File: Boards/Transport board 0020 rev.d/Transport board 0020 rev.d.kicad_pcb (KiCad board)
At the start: 2 copper layers, 165.9 x 187.4 mm, 82 parts, among them P1 CEC card edge connector large, U1 TR1602, U10 LM311, U11 LM741, U12 LM311, U14 Spare, U15 Spare, U2 6821, U3 DM8602N, U4 7410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

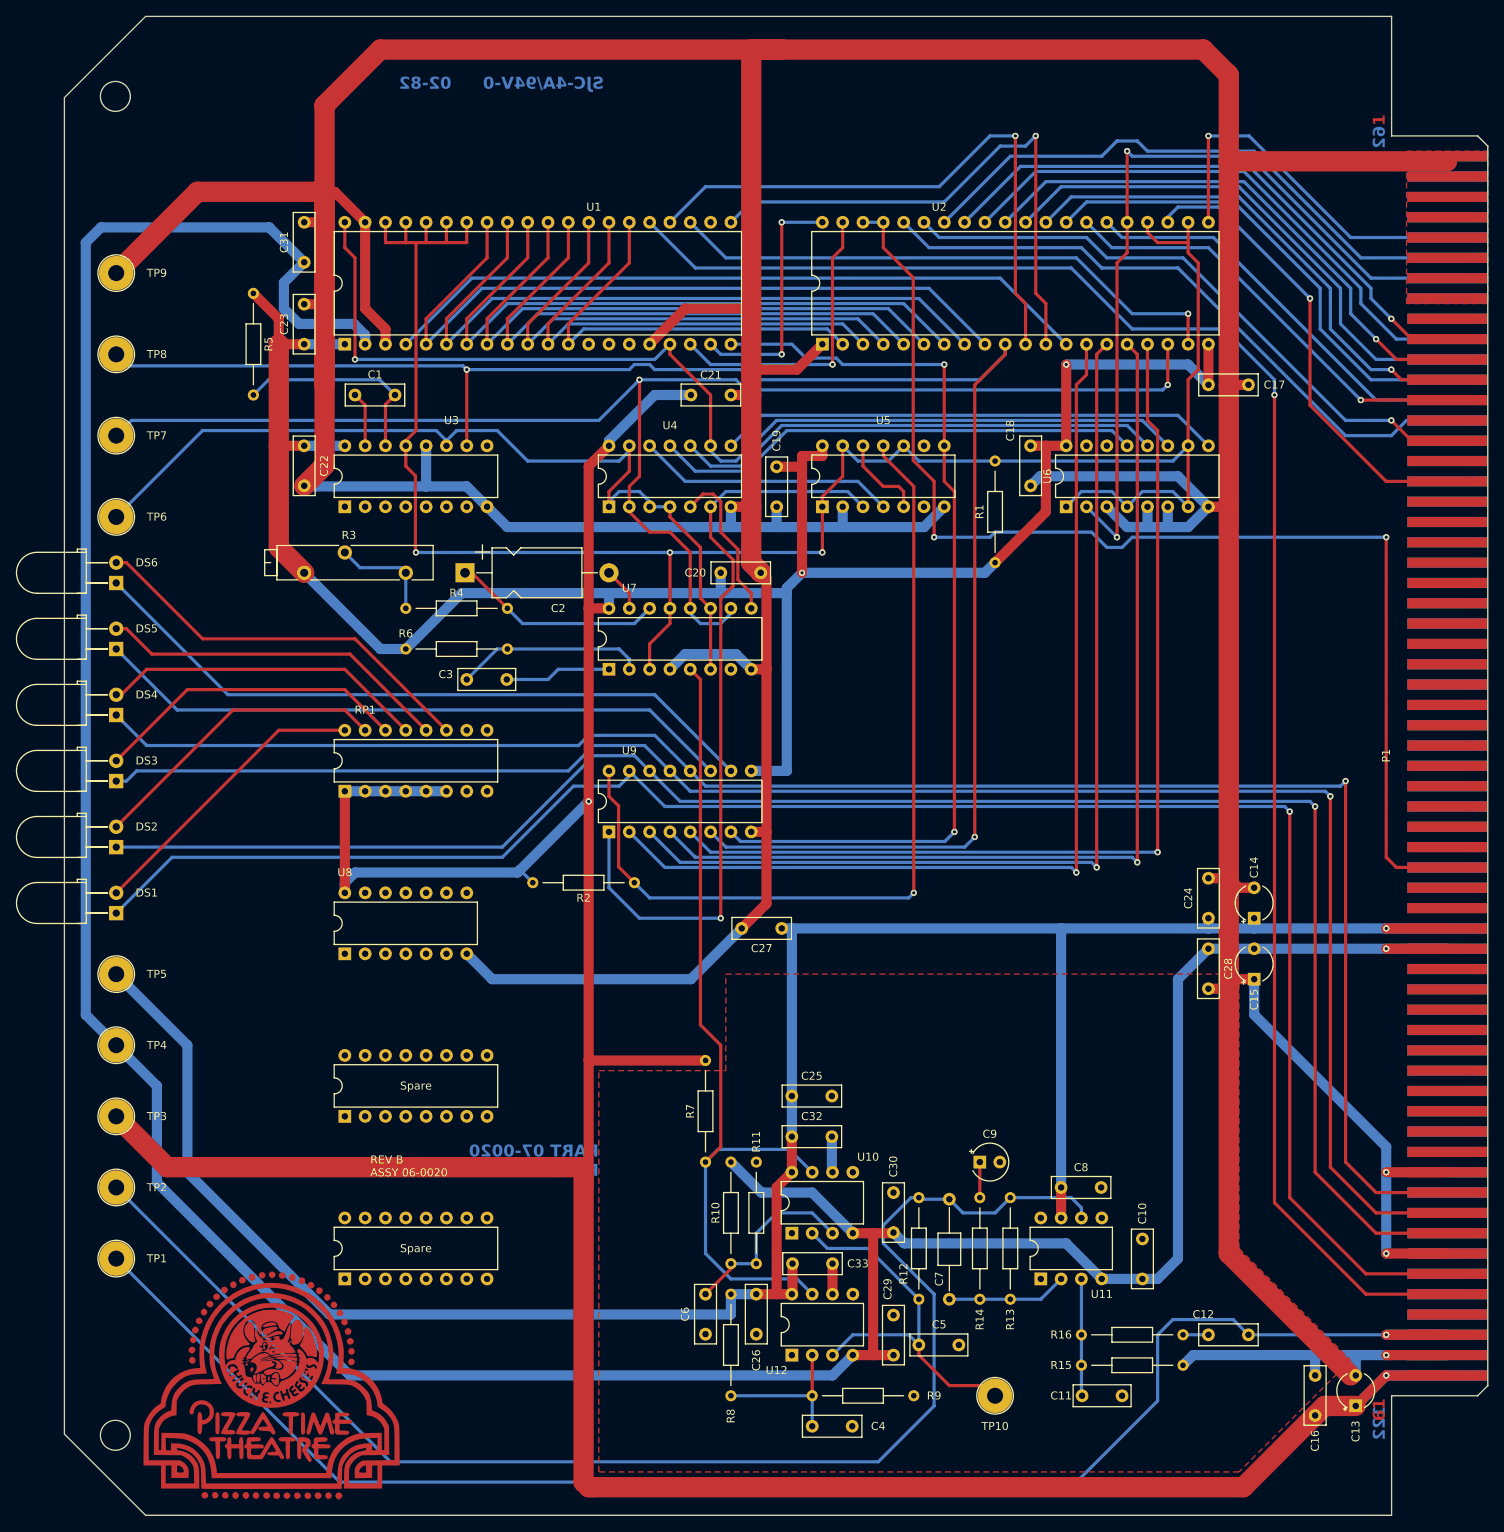
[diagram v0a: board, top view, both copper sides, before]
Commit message: Fix spelling errors with Transport
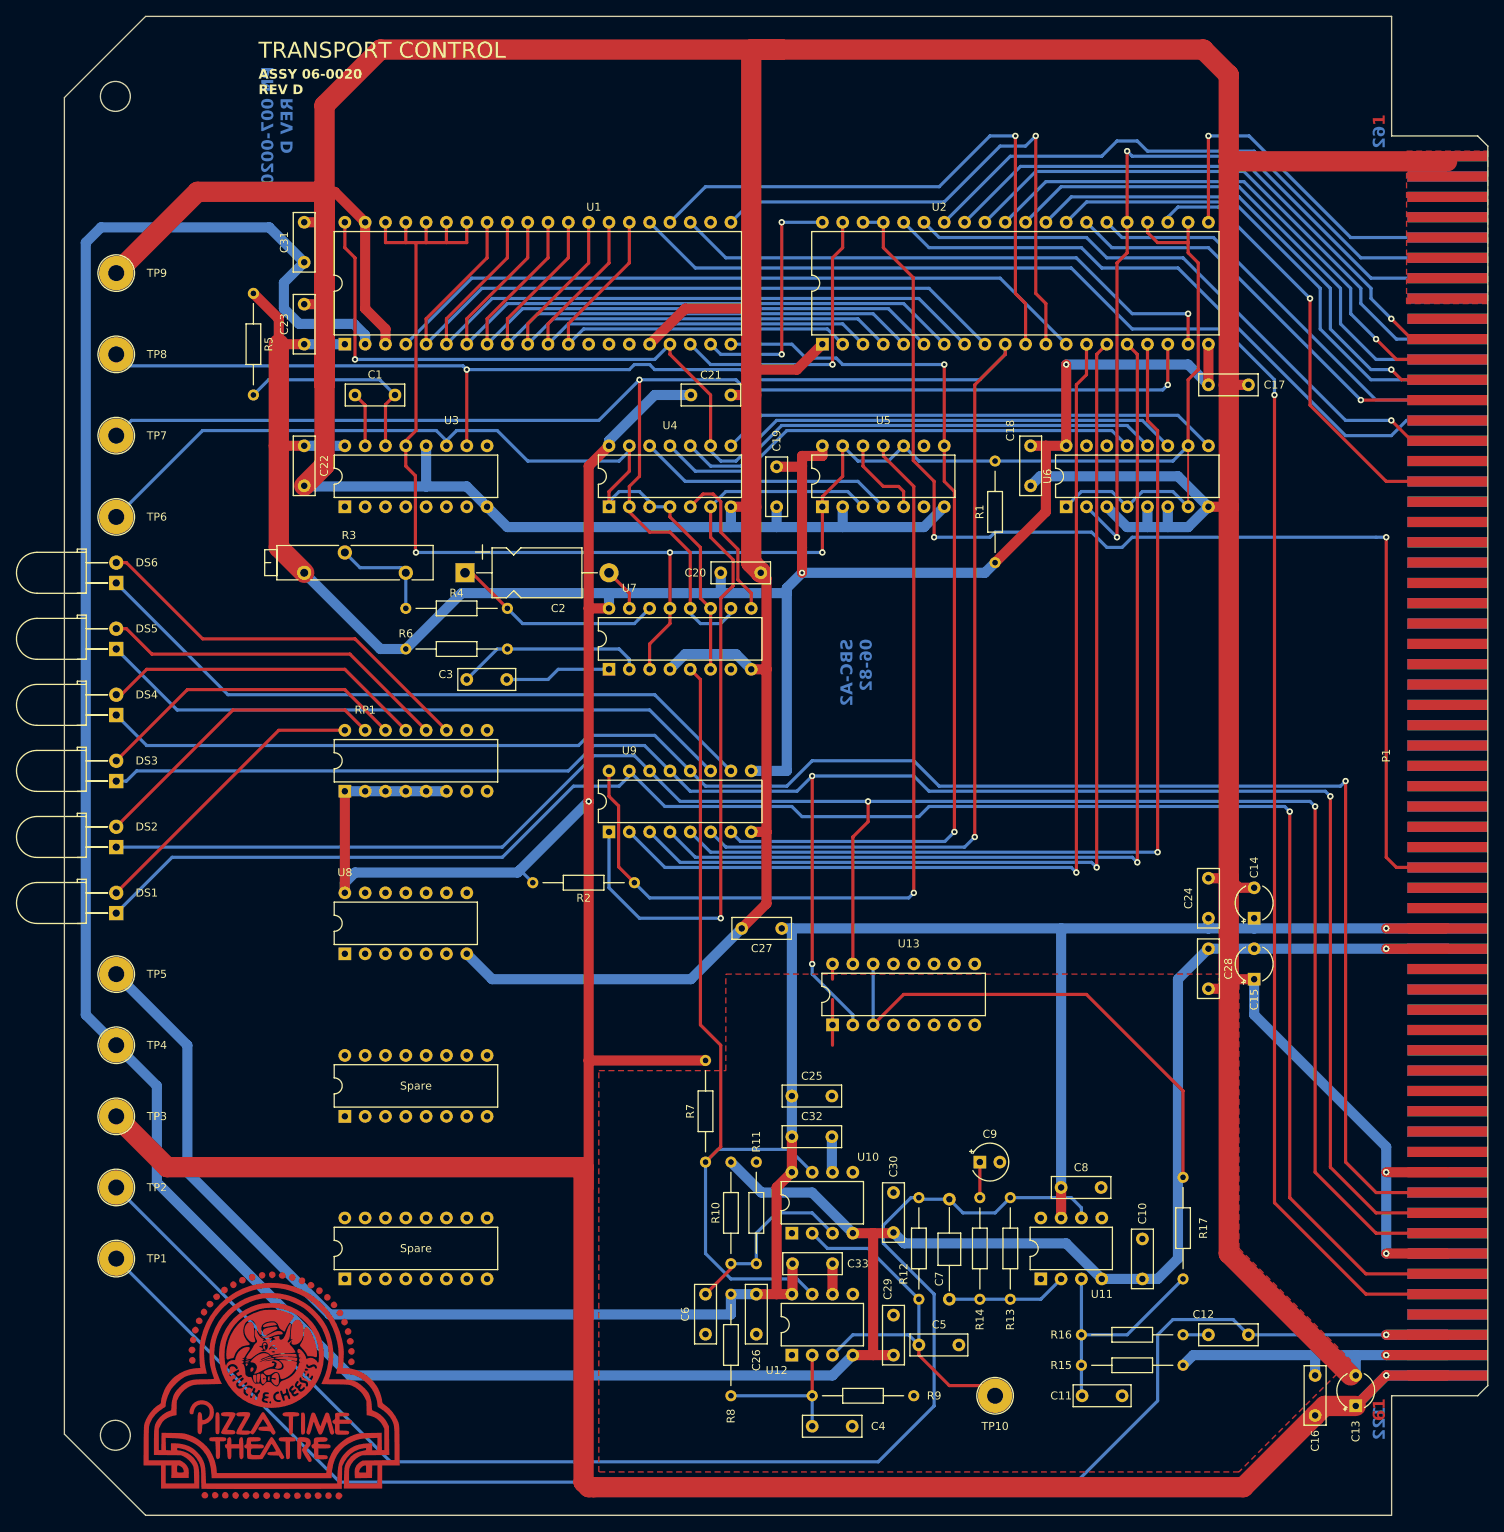
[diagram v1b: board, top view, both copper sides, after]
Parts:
- added R17: 2.2K, Evan's parts:R_Axial_DIN0204_L3.6mm_D1.6mm_P12.7mm_Horizontal, F.Cu at (162.6, 167.6)
- added U13: AH5012, Package_DIP:DIP-16_W7.62mm, F.Cu at (118.7, 138.4)
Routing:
- net Net-(R17-Pad2): track 0.00 -> 63.7 mm
- net R.W.: track 219.6 -> 254.4 mm, vias 1 -> 3
- net F.F.: track 222.6 -> 243.7 mm, vias 1 -> 2
- net Net-(U11-+): track 14.6 -> 30.2 mm
- net GND: track 903.6 -> 911.2 mm
- net PLAY: track 220.6 -> 223.2 mm
- net STOP: track 228.4 -> 229.5 mm
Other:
- board text added: "ASSY 06-0020 REV D"
- board text added: "PN 007-0020 REV D"
- board text added: "SBC-A2 06-82"
- board text added: "TRANSPORT CONTROL"
- board text removed: "02-82"
- board text removed: "PART 07-0020 REV B"
- board text removed: "REV B ASSY 06-0020"
- board text removed: "SJC-4A/94V-0"

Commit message: transport board silk update
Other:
- board text added: "Spare"
